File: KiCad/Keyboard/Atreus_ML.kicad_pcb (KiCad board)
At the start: 2 copper layers, 252 x 101 mm, 85 parts, among them K1 CHERRY_ML, K10 CHERRY_ML, K11 CHERRY_ML, K12 CHERRY_ML, K13 CHERRY_ML, K14 CHERRY_ML, K15 CHERRY_ML, K16 CHERRY_ML, K17 CHERRY_ML, K18 CHERRY_ML, K19 CHERRY_ML, K2 CHERRY_ML, K20 CHERRY_ML, K21 CHERRY_ML, K22 CHERRY_ML, K23 CHERRY_ML, K24 CHERRY_ML, K25 CHERRY_ML, K26 CHERRY_ML, K27 CHERRY_ML, K28 CHERRY_ML, K29 CHERRY_ML, K3 CHERRY_ML, K30 CHERRY_ML, K31 CHERRY_ML, K32 CHERRY_ML, K33 CHERRY_ML, K34 CHERRY_ML, K35 CHERRY_ML, K36 CHERRY_ML, K37 CHERRY_ML, K38 CHERRY_ML, K39 CHERRY_ML, K4 CHERRY_ML, K40 CHERRY_ML, K41 CHERRY_ML, K42 CHERRY_ML, K5 CHERRY_ML, K6 CHERRY_ML, K7 CHERRY_ML, K8 CHERRY_ML, K9 CHERRY_ML, U1 TEENSY2.0-Compact

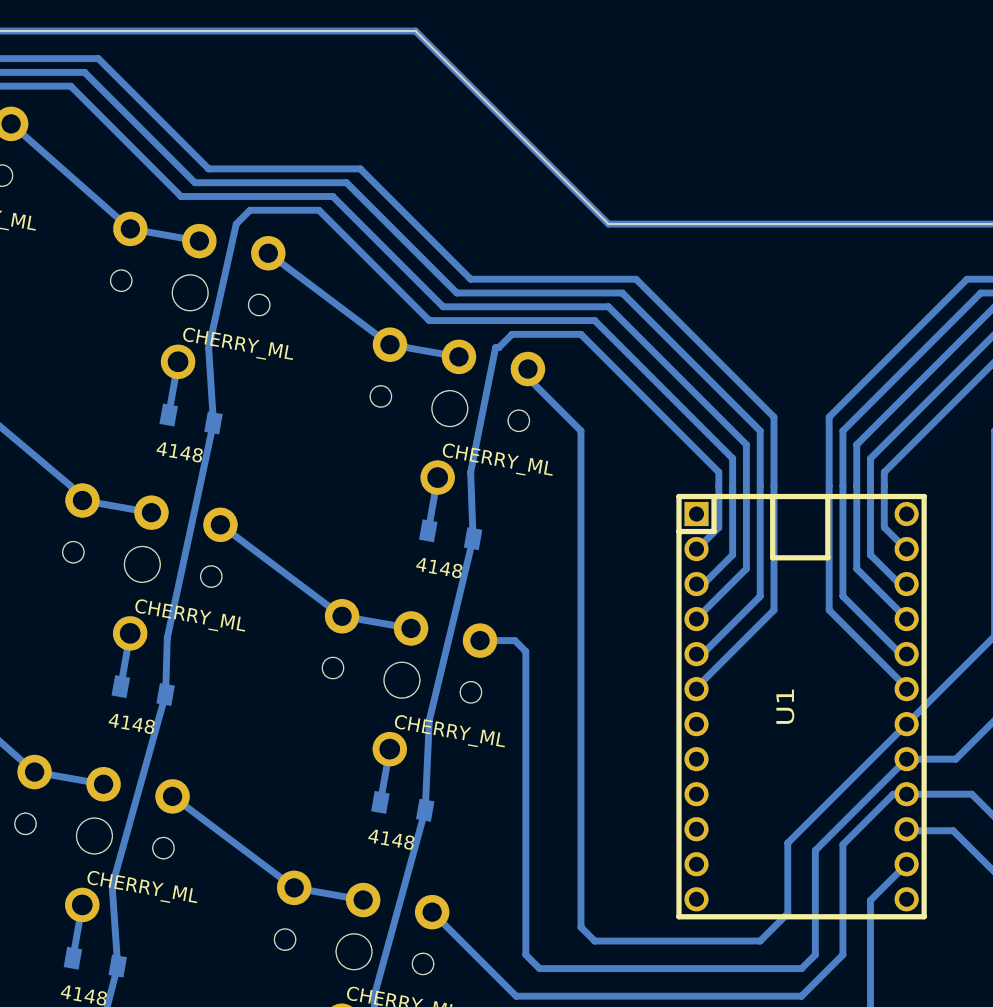
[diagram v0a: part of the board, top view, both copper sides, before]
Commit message: Rev 3, now with headers for unused pins
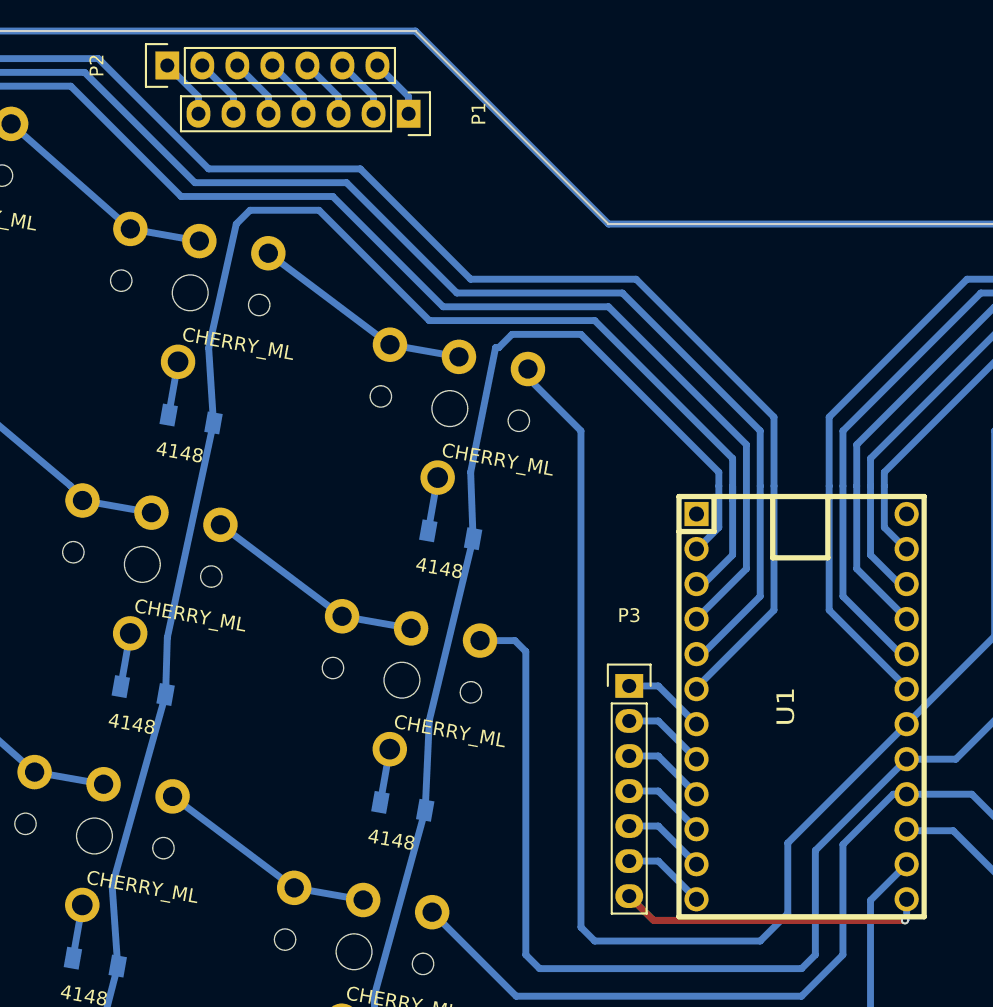
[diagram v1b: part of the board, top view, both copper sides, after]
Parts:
- added P1: CONN_01X07, Pin_Headers:Pin_Header_Straight_1x07, F.Cu at (121.5, 55.0)
- added P2: CONN_01X07, Pin_Headers:Pin_Header_Straight_1x07, F.Cu at (104.0, 51.5)
- added P3: CONN_01X07, Pin_Headers:Pin_Header_Straight_1x07, F.Cu at (137.5, 96.5)
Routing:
- net Net-(P3-Pad7): track 0.00 -> 22.3 mm, vias 0 -> 2
- net Net-(P3-Pad5): track 0.00 -> 6.03 mm
- net Net-(P3-Pad6): track 0.00 -> 6.03 mm
- net Net-(P3-Pad4): track 0.00 -> 6.03 mm
- net Net-(P3-Pad3): track 0.00 -> 6.03 mm
- net Net-(P3-Pad2): track 0.00 -> 6.03 mm
- net Net-(P3-Pad1): track 0.00 -> 6.03 mm
- net Net-(P1-Pad7): track 0.00 -> 4.44 mm
- net Net-(P1-Pad5): track 0.00 -> 4.44 mm
- net Net-(P1-Pad3): track 0.00 -> 4.44 mm
- net Net-(P1-Pad1): track 0.00 -> 4.44 mm
- net Net-(P1-Pad6): track 0.00 -> 4.44 mm
- net Net-(P1-Pad4): track 0.00 -> 4.44 mm
- net Net-(P1-Pad2): track 0.00 -> 4.44 mm

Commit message: Rev 4
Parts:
- K1, K10, K11, K12, K13, K14, K15, K16, K17, K18, K19, K2, K20, K21, K22, K23, K24, K25, K26, K27, K28, K29, K3, K30, K31, K32, K33, K34, K35, K36, K37, K38, K39, K4, K40, K41, K42, K5, K6, K7, K8, K9: footprint CHERRY_ML:CHERRY_ML -> Cherry_ML:CHERRY_ML_Etch
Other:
- outline, holes or cut-outs redrawn

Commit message: Fixing design whoopsie
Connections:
- K1 pad 3: Net-(K1-Pad3) -> Net-(K1-Pad1)
- K2 pad 3: Net-(K2-Pad3) -> Net-(K2-Pad1)
- K21 pad 4: Net-(K21-Pad4) -> Net-(K21-Pad1)
- K22 pad 1: Net-(K22-Pad1) -> Net-(K21-Pad1)
- K22 pad 3: Net-(K21-Pad4) -> Net-(K21-Pad1)
- K3 pad 3: Net-(K3-Pad3) -> Net-(K3-Pad1)
- K39 pad 4: Net-(K39-Pad4) -> Net-(K39-Pad1)
- K4 pad 3: Net-(K4-Pad3) -> Net-(K4-Pad1)
- K40 pad 4: Net-(K40-Pad4) -> Net-(K40-Pad1)
- K41 pad 4: Net-(K41-Pad4) -> Net-(K41-Pad1)
- K42 pad 4: Net-(K42-Pad4) -> Net-(K42-Pad1)
- U1 pad 19: Net-(K21-Pad4) -> Net-(K21-Pad1)
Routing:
- net Net-(K21-Pad1): track 0.00 -> 47.3 mm
- net Net-(K21-Pad4): track 37.1 -> 0.00 mm
- net Net-(K4-Pad1): track 0.00 -> 5.08 mm
- net Net-(K39-Pad1): track 0.00 -> 5.08 mm
- net Net-(K3-Pad1): track 0.00 -> 5.08 mm
- net Net-(K2-Pad1): track 0.00 -> 5.08 mm
- net Net-(K1-Pad1): track 0.00 -> 5.08 mm
- net Net-(K42-Pad1): track 0.00 -> 5.08 mm
- net Net-(K41-Pad1): track 0.00 -> 5.08 mm
- net Net-(K40-Pad1): track 0.00 -> 5.08 mm
